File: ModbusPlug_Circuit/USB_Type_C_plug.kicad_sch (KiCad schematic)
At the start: 1 part, among them J1 USB4155-03-C_REVA

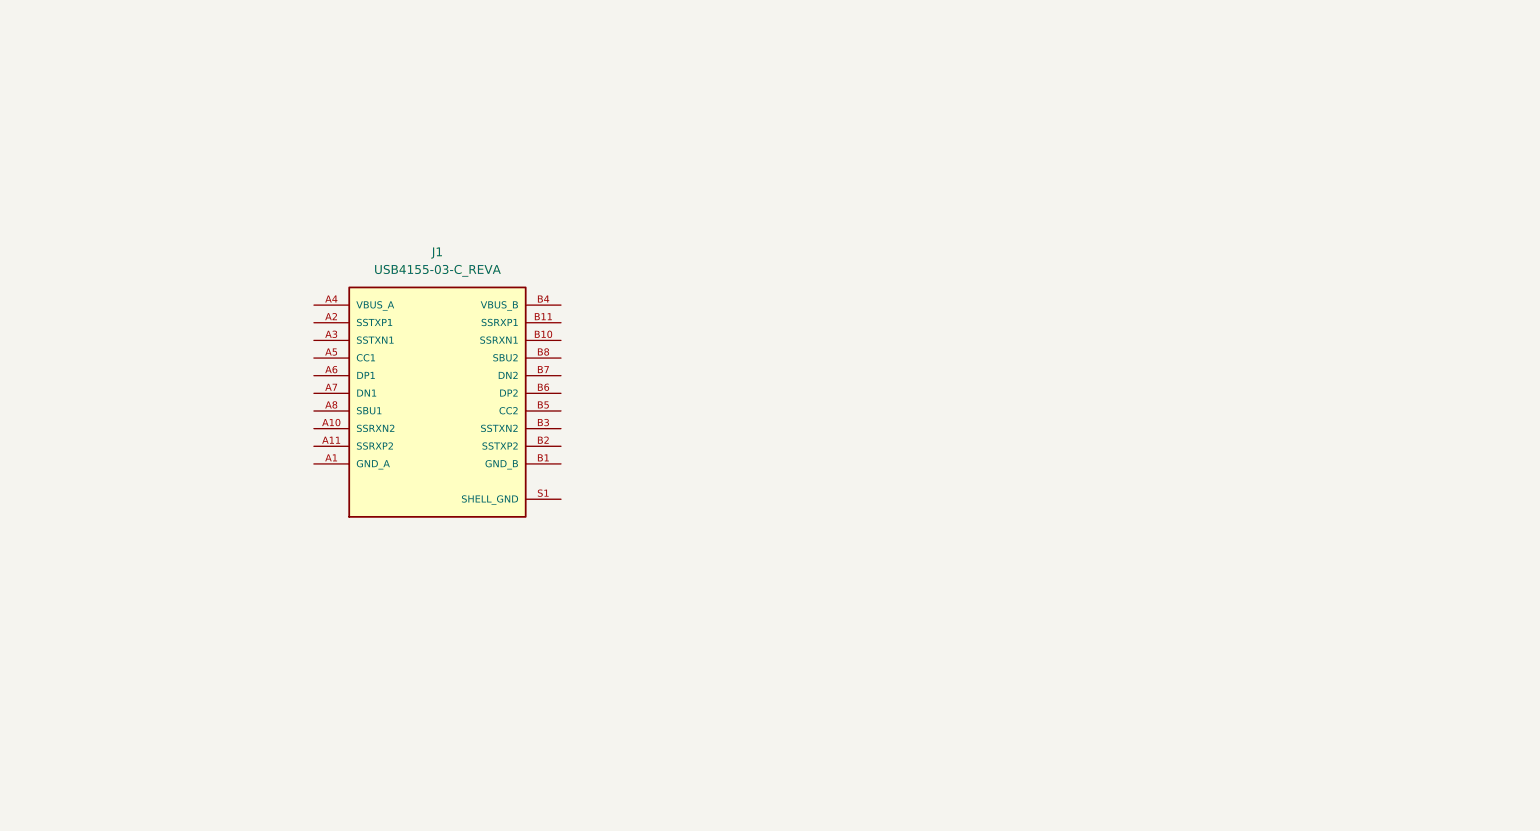
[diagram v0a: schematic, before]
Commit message: Updated USB/PD and TTL circuit
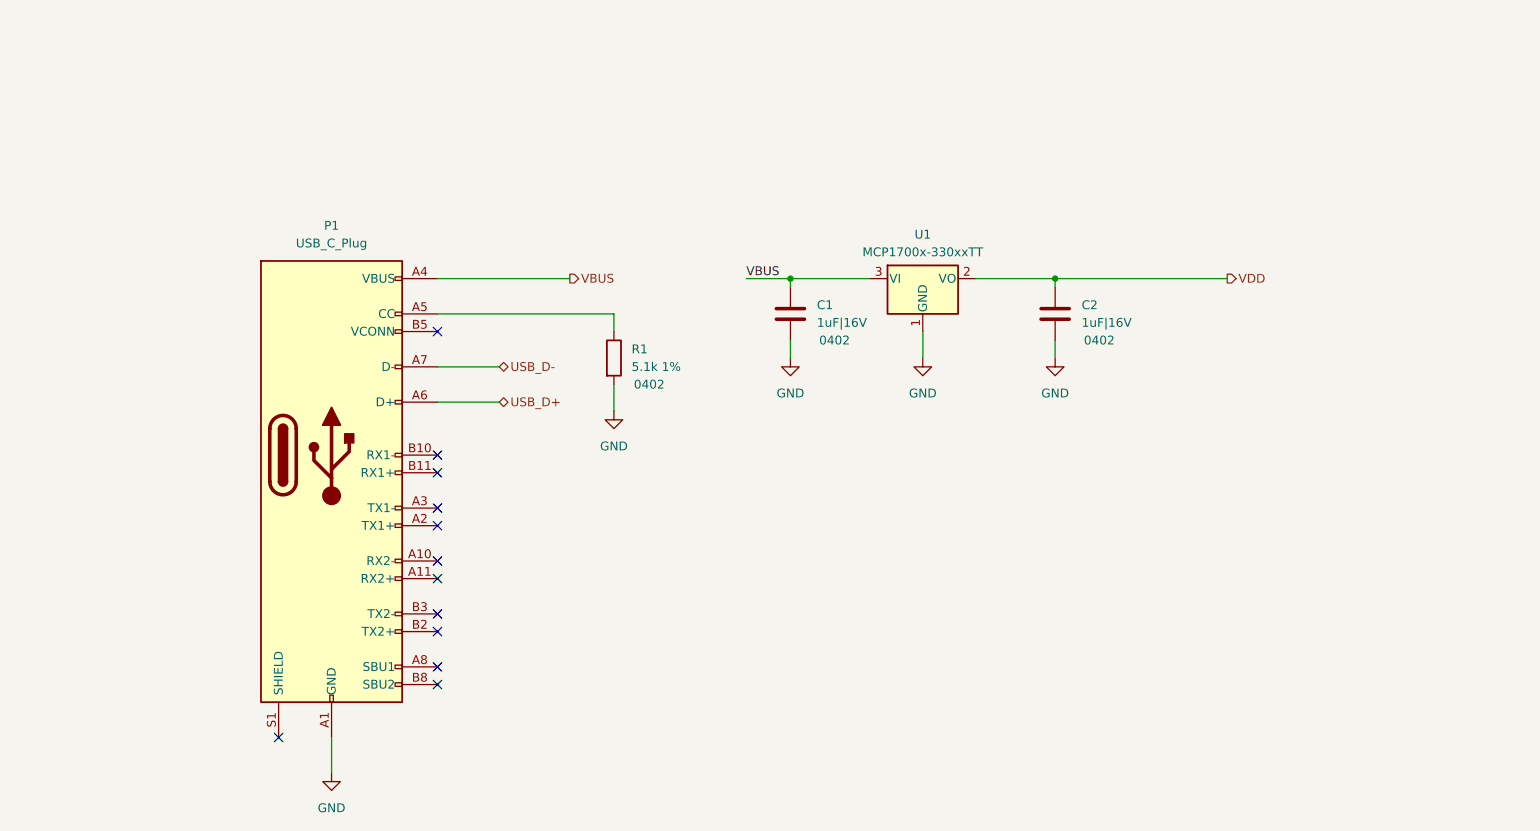
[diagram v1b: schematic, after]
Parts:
- added C1, C2: 1uF|16V, Capacitor_SMD:C_0402_1005Metric, symbol Device:C
- added R1: 5.1k 1%, Resistor_SMD:R_0402_1005Metric, symbol Device:R
- added U1: MCP1700x-330xxTT, Package_TO_SOT_SMD:SOT-23, symbol Regulator_Linear:MCP1700x-330xxTT
- P1: renamed from J1; value USB4155-03-C_REVA -> USB_C_Plug; footprint USB4155-03-C_REVA:GCT_USB4155-03-C_REVA -> Footprint:GCT_USB4155-03-C_REVA; symbol USB4155-03-C_REVA:USB4155-03-C_REVA -> Connector:USB_C_Plug
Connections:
- net GND_B is gone; now on net GND: P1.B1 (GND), P1.B12 (GND)
- net VBUS_B is gone; now on net VBUS: P1.B4 (VBUS), P1.B9 (VBUS)
- net at P1.A5 (CC): now also R1.1
- net USB_D+: now reaches P1.A6 (D+)
- net USB_D+: now also P1.B6 (D+)
- net USB_D-: now reaches P1.A7 (D-)
- net USB_D-: now also P1.B7 (D-)
- net GND_A renamed GND
- net GND: now also C1.2, C2.2, R1.2, U1.1 (GND)
- net SHELL_GND: no longer names the net of P1.S1 (SHIELD)
- net SHELL_GND: no longer P1.S2 (SHELL_GND)
- net VBUS_A renamed VBUS
- net VBUS: now also C1.1, U1.3 (VI)
- new net VDD: C2.1, U1.2 (VO)
- no-connect marks 0 -> 12

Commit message: pushing V0.1
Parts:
- added U4: USBLC6-2SC6, Package_TO_SOT_SMD:SOT-23-6, symbol Power_Protection:USBLC6-2SC6
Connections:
- net GND: now also U4.2 (GND)
- net USB_D+: now also U4.4 (I/O2); no longer P1.A6 (D+), P1.B6 (D+)
- net USB_D-: now also U4.6 (I/O1); no longer P1.A7 (D-), P1.B7 (D-)
- net VBUS: now also U4.5 (VBUS)
- new net D+: P1.A6 (D+), P1.B6 (D+), U4.3 (I/O2)
- new net D-: P1.A7 (D-), P1.B7 (D-), U4.1 (I/O1)
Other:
- moved on the sheet: C1, C2, R1, U1

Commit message: pushing V0.1.1
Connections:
- net VBUS renamed VBUS_out
- net VDD renamed 3.3V_out
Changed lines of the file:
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@@
 	(wire
 		(pts
-			(xy 196.85 53.34) (xy 221.615 53.34)
+			(xy 196.85 53.34) (xy 220.98 53.34)
 		)
 		(stroke
@@
 		)
 	)
-	(label "VBUS"
+	(label "VBUS_out"
 		(at 100.33 60.96 180)
 		(effects
@@
 		)
 	)
-	(label "VBUS"
+	(label "VBUS_out"
 		(at 152.4 53.34 0)
 		(effects
@@
 		)
 	)
-	(hierarchical_label "VDD"
-		(shape output)
-		(at 221.615 53.34 0)
-		(effects
-			(font
-				(size 1.27 1.27)
-			)
-			(justify left)
-		)
-	)
 	(hierarchical_label "USB_D+"
 		(shape bidirectional)
@@
 		)
 	)
-	(hierarchical_label "VBUS"
+	(hierarchical_label "VBUS_out"
 		(shape output)
 		(at 127 53.34 0)
 		(effects
 			(font
+				(size 1.27 1.27)
+			)
+			(justify left)
+		)
+	)
+	(hierarchical_label "3.3V_out"
+		(shape output)
+		(at 220.98 53.34 0)
+		(effects
+			(font

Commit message: pushin V0.1.2
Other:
- moved on the sheet: C1, C2, P1, R1, U1, U4

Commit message: pushing V0.1.4
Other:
- title: (none) -> ModbusPlug
- moved on the sheet: C1, C2, P1, R1, U1, U4
